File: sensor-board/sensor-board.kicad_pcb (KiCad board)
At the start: 2 copper layers, 41.5 x 40 mm, 12 parts, among them J1 SM04B-SRSS-TB, U1 HDC2010YPAR, U2 HP203B

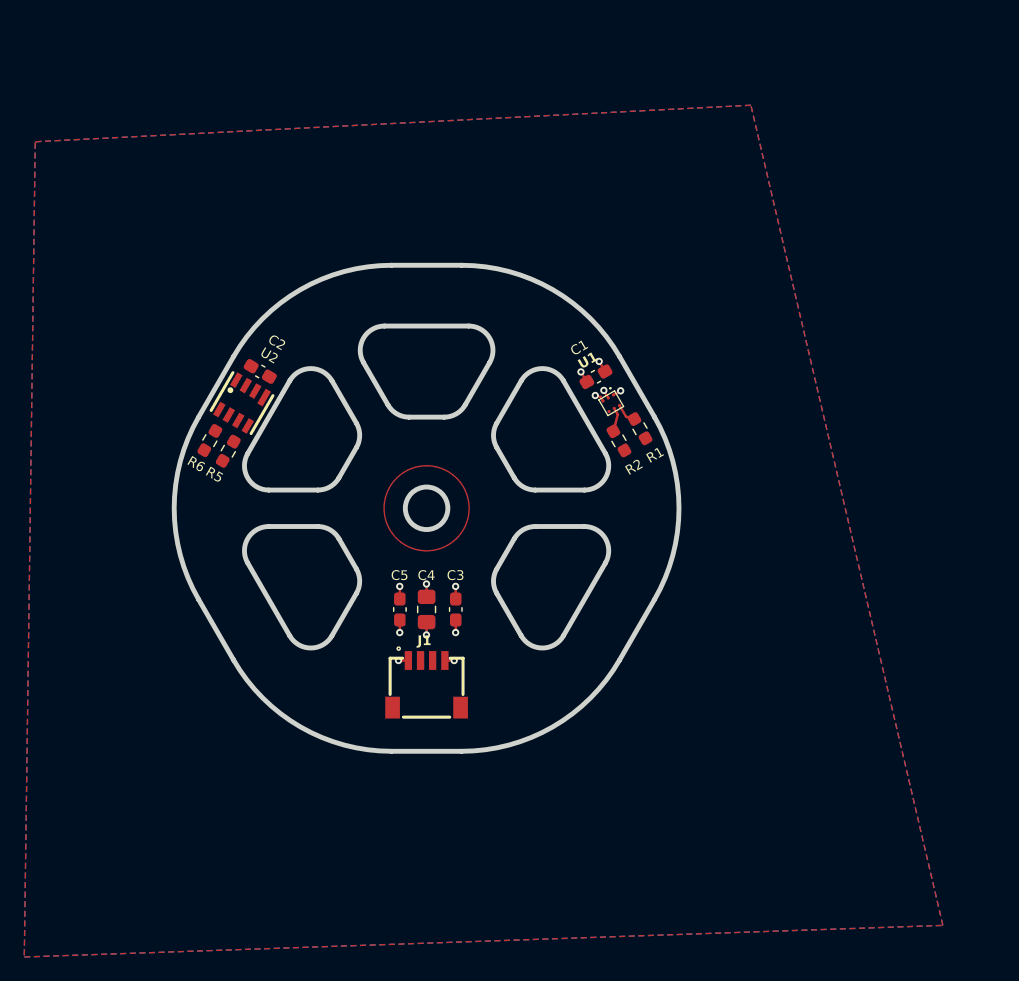
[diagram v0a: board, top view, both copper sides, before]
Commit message: sensor-board: Finalize the first iteration
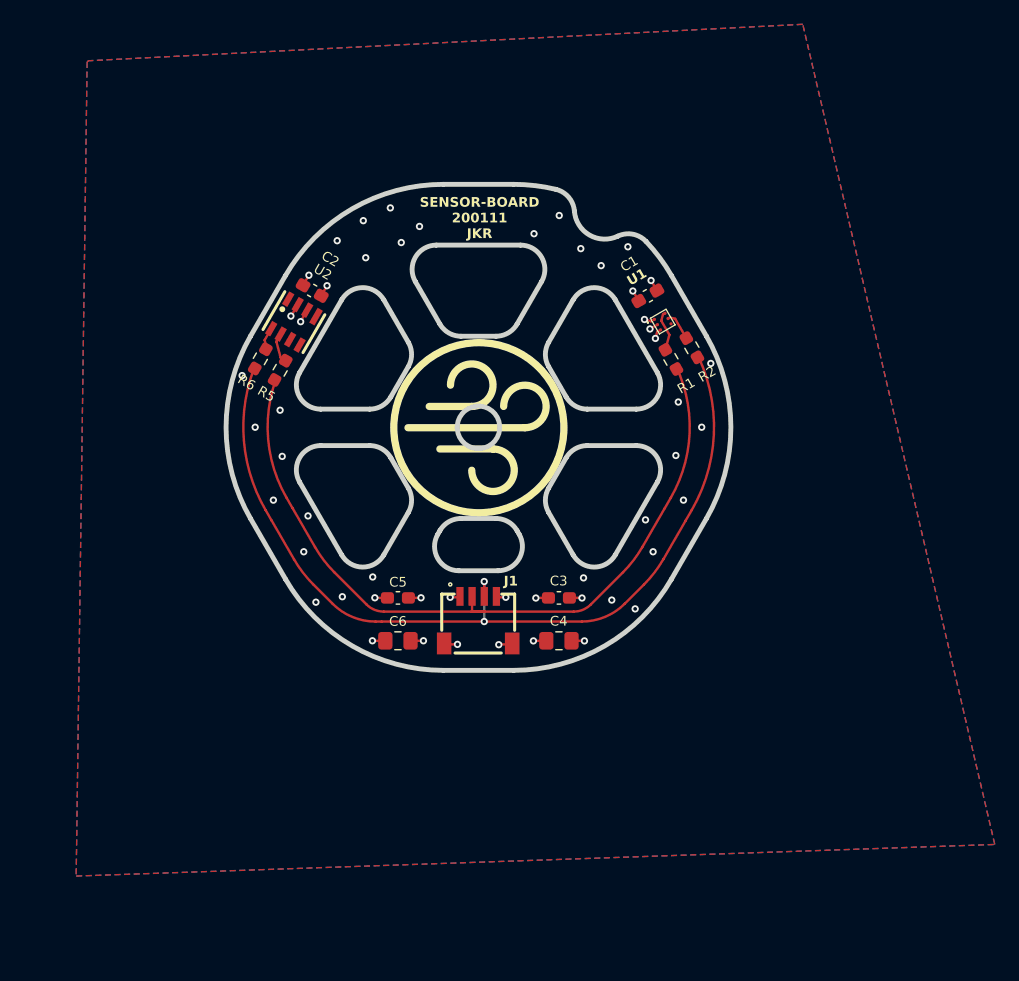
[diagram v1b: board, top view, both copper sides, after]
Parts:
- added C6: 22u, njordr:C-0805-HandSolder, F.Cu at (148.8, 107.6)
- J1: value SM04B-SRSS-TB -> SM04B-SRSS-TB(LFSN)
- moved C4 11.2 mm to (162.0, 107.6), turned to 180 degrees
- moved J1 10.5 mm to (155.4, 106.3)
- moved R2 9.73 mm to (172.9, 83.5)
- moved C3 8.54 mm to (162.0, 104.0), turned to 180 degrees
- moved U1 7.94 mm to (170.5, 81.3), turned to 30 degrees
- moved C1 7.91 mm to (169.3, 79.2)
- moved R5 7.91 mm to (139.1, 85.3)
- moved C2 7.91 mm to (141.7, 78.8)
- moved U2 7.91 mm to (140.2, 81.3)
- moved R6 7.91 mm to (137.4, 84.4)
- moved R1 6.25 mm to (171.2, 84.4)
- moved C5 0.97 mm to (148.7, 104.0), turned to 0 degrees
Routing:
- net /SCL: track 0.00 -> 46.5 mm, vias 0 -> 2
- net /SDA: track 0.00 -> 41.1 mm
- net GND: track 6.43 -> 11.8 mm, vias 7 -> 43
- net VCC: track 5.60 -> 8.92 mm, vias 6 -> 9
- net Net-(U2-SDA): track 0.00 -> 2.57 mm
- net Net-(U2-SCL): track 0.00 -> 1.94 mm
- net Net-(U1-SDA): track 1.79 -> 3.34 mm
- added copper zone on In1.Cu, net GND
- added copper zone on In2.Cu, net VCC
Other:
- outline, holes or cut-outs redrawn
- copper layers 2 -> 4
- board text added: "SENSOR-BOARD 200111 JKR"
